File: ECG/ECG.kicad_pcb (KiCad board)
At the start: 4 copper layers, 81.3 x 109.2 mm, 85 parts, among them J1 Conn_01x03, J17 Conn_02x04_Odd_Even, J2 Conn_01x03, J3 Conn_02x15_Odd_Even, J4 Conn_02x15_Odd_Even, J5 Conn_01x02, J6 Conn_01x02, J7 Conn_01x03, J8 Conn_02x05_Odd_Even, Q1 DMG2301L, Q2 T2N7002AK, Q3 T2N7002AK, Q4 T2N7002AK, Q5 T2N7002AK, Q6 T2N7002AK, U1 AD8232ACPZ-R7, U2 MIC920YC5-TR, U3 ABX00027

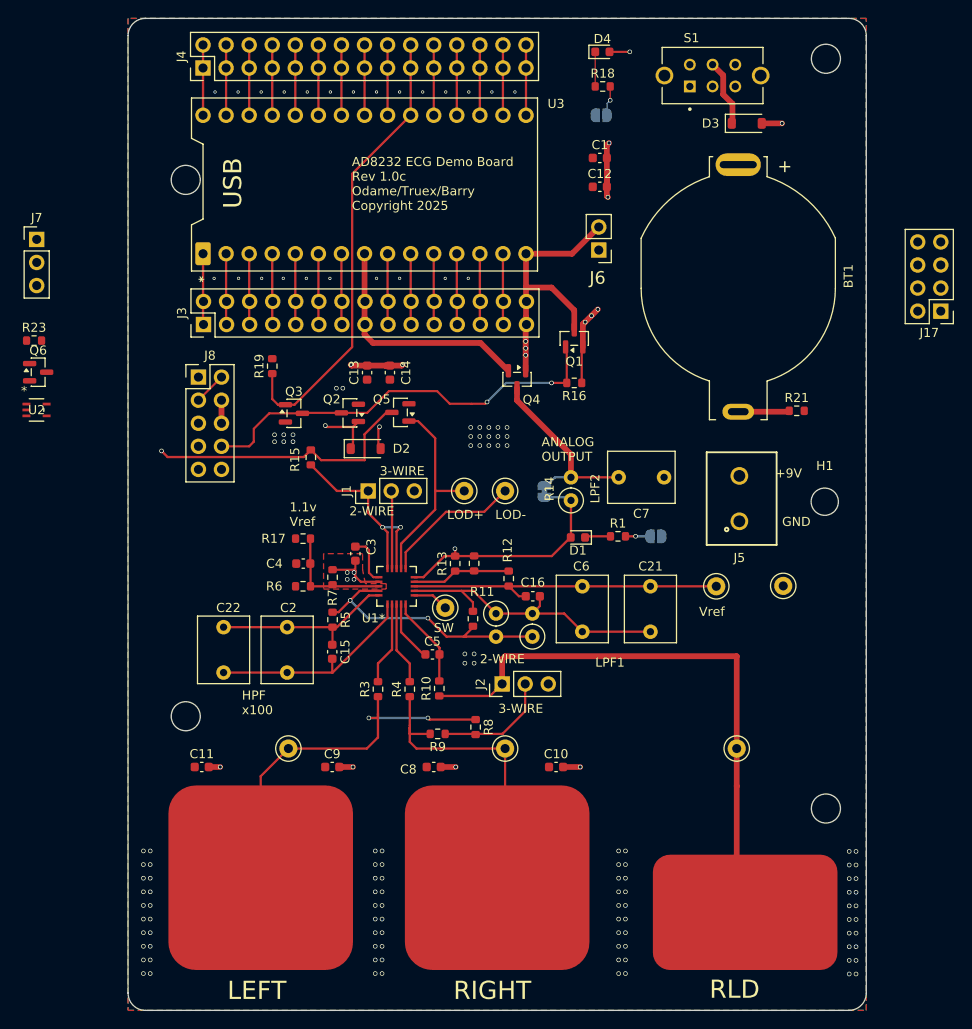
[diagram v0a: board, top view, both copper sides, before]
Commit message: Replace high leakage op-amp with slower low power variant to minimize input current requirements.
Close #25
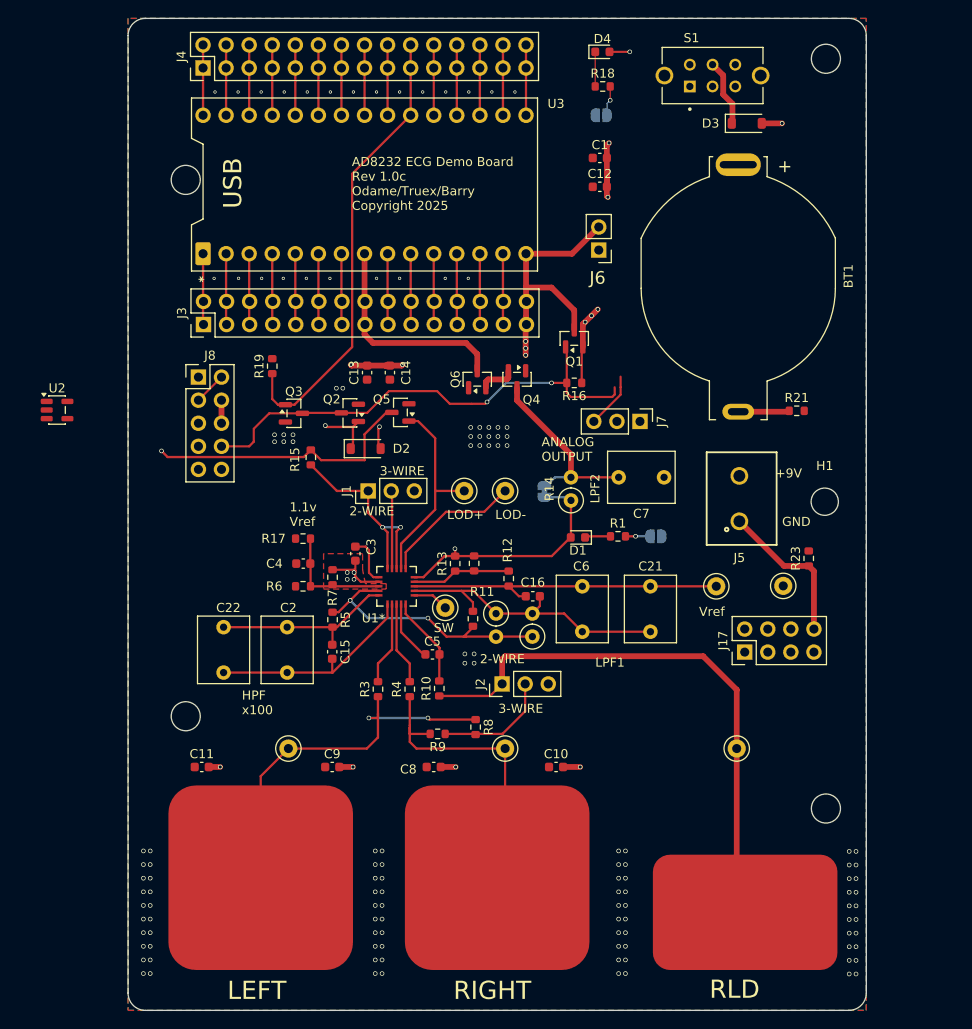
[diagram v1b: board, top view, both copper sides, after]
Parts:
- U2: value MIC920YC5-TR -> LMC7101BYM5; footprint StockedComponents:SC-70_C5_MCH -> Package_TO_SOT_SMD:SOT-23-5
- moved R23 88.6 mm to (167.0, 84.2), turned to 90 degrees
- moved J7 69.4 mm to (148.4, 69.1), turned to -90 degrees
- moved Q6 48.4 mm to (130.5, 64.5), turned to 90 degrees
- moved J17 43.3 mm to (160.0, 94.5), turned to 90 degrees
- moved U2 2.26 mm to (84.3, 67.9)
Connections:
- U2 pad 1: /PWR_OFF_HV -> /PWR_OFF_BUF
- U2 pad 2: GND -> +9V
- U2 pad 3: /PWR_OFF_BUF -> /PWR_OFF_HV
- U2 pad 5: +9V -> GND
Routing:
- net +9V: track 47.4 -> 128.2 mm
- net +3V0: track 37.1 -> 106.0 mm
- net /3VSens: track 5.66 -> 32.7 mm
- net /9VSens: track 0.00 -> 16.9 mm
- net /PWR_OFF_HV: track 46.9 -> 54.4 mm
- net GND: track 20.7 -> 26.8 mm
- net Net-(Q4-S): track 0.00 -> 4.09 mm
- net /HR_SIGNAL: track 37.2 -> 34.8 mm
- net /RL: track 64.6 -> 62.4 mm
- net /VIN: track 46.6 -> 44.9 mm
- net Net-(D3-A): track 46.0 -> 44.5 mm

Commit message: First shot at P&R for these edits.
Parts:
- removed C21, C22: DNP, Capacitor_THT:C_Rect_L7.2mm_W5.5mm_P5.00mm_FKS2_FKP2_MKS2_MKP2
- removed R22: DNP, Resistor_THT:R_Axial_DIN0207_L6.3mm_D2.5mm_P2.54mm_Vertical
- moved U2 62.5 mm to (146.6, 63.8), turned to -90 degrees
- moved TP7 8.66 mm to (148.2, 87.2)
- turned Q6 to -90 degrees
- turned R23 to -90 degrees
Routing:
- net /PWR_OFF_BUF: track 0.00 -> 53.7 mm, vias 0 -> 1
- net Net-(J7-Pin_2): track 0.00 -> 20.1 mm
- net /REF: track 35.6 -> 27.0 mm
- net /OAP: track 33.5 -> 26.0 mm
- net /HPSENSE: track 20.5 -> 13.5 mm
- net /HPDRIVE: track 23.6 -> 16.6 mm
- net +9V: track 128.2 -> 135.2 mm, vias 3 -> 4
- net /PWR_OFF_HV: track 54.4 -> 48.0 mm
- net GND: track 26.8 -> 20.7 mm, vias 131 -> 107
- net /IAOUT: track 29.8 -> 25.6 mm
- net /9VSens: track 16.9 -> 20.8 mm
- net Net-(Q4-S): track 4.09 -> 7.16 mm
- net /HR_SIGNAL: track 34.8 -> 37.5 mm

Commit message: add socket for arduino into bom.  exclude arduino from board.
Add decap for new op-amp.

Close #39
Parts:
- removed U3: ABX00027, ECG_Footprints:DIP30-ArduinoNano
- added C17: 100nF, Capacitor_SMD:C_0603_1608Metric, F.Cu at (146.6, 58.4)
- added J10: Socket 1x15, Connector_PinSocket_2.54mm:PinSocket_1x15_P2.54mm_Vertical, F.Cu at (100.3, 50.7)
- added J9: Socket 1x15, Connector_PinSocket_2.54mm:PinSocket_1x15_P2.54mm_Vertical, F.Cu at (100.3, 35.4)
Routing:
- net +9V: track 135.2 -> 137.0 mm

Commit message: Add new QR code.
Close #32
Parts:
- G***: footprint ECG_Footprints:ECG_V1.0c -> ECG_Footprints:ECG_V1.1
